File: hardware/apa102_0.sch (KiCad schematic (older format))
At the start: 77 parts

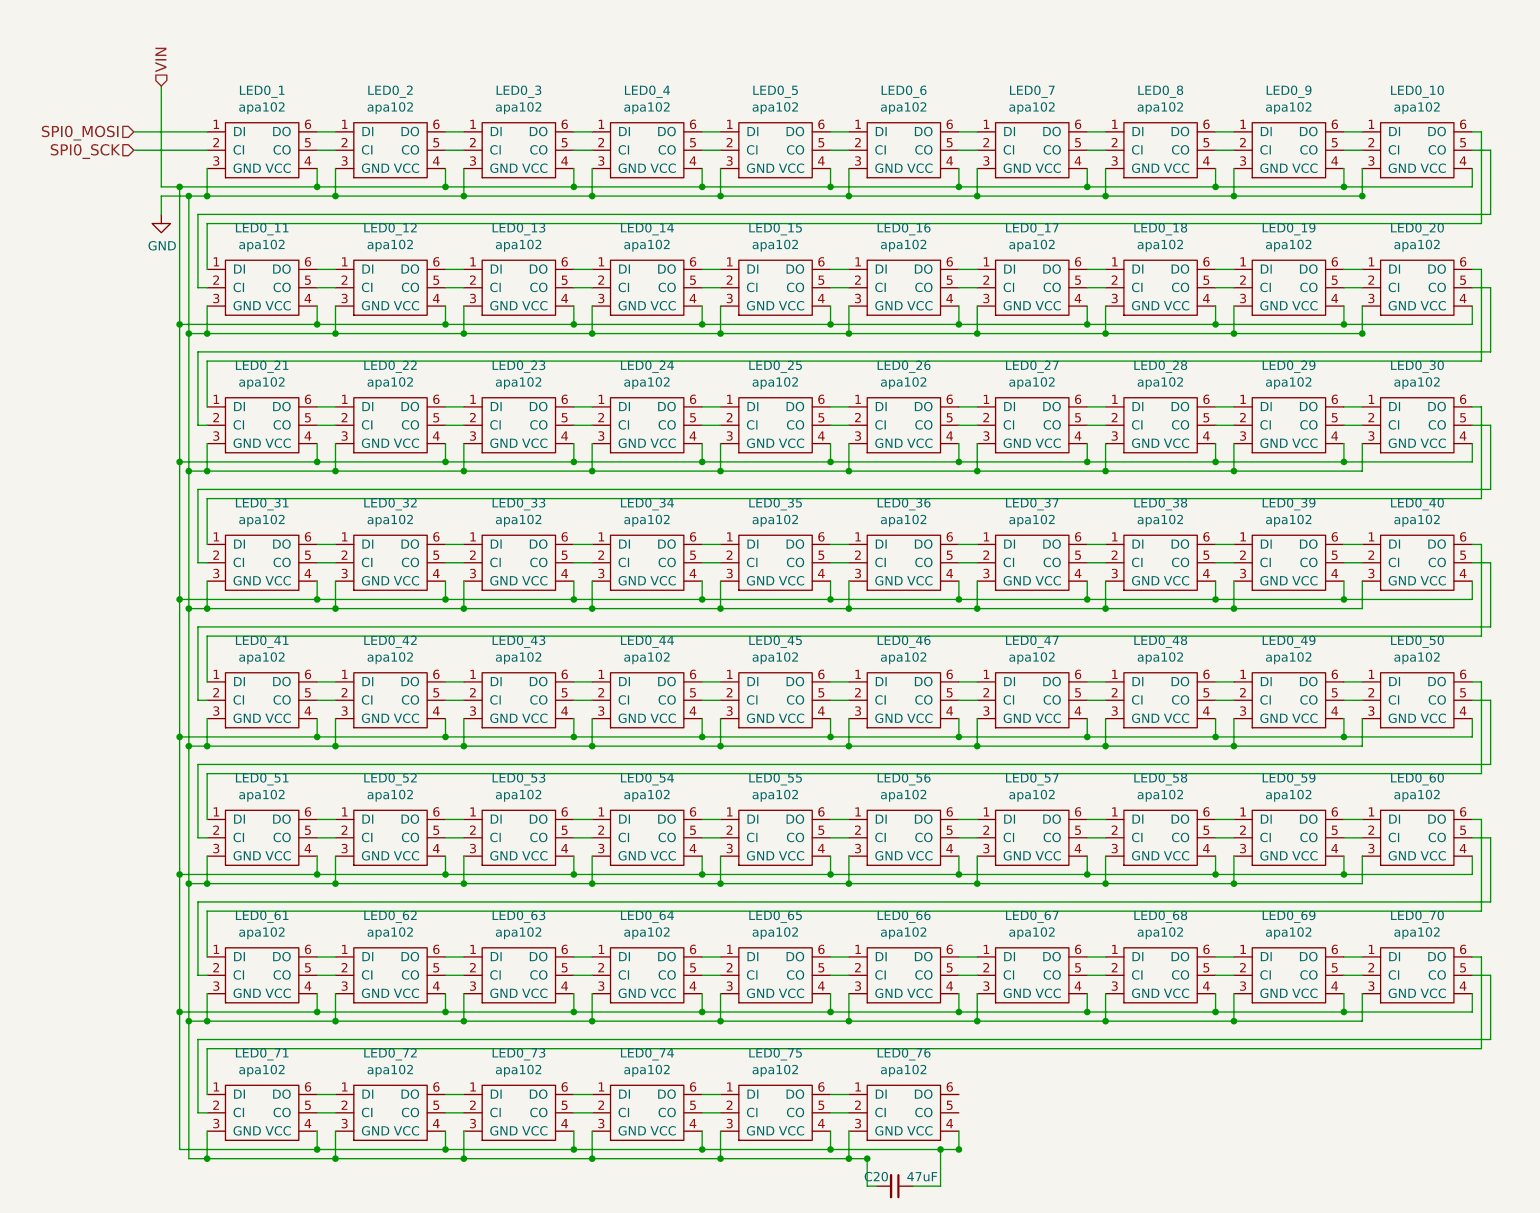
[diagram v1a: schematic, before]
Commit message: Removed 72 LEDs
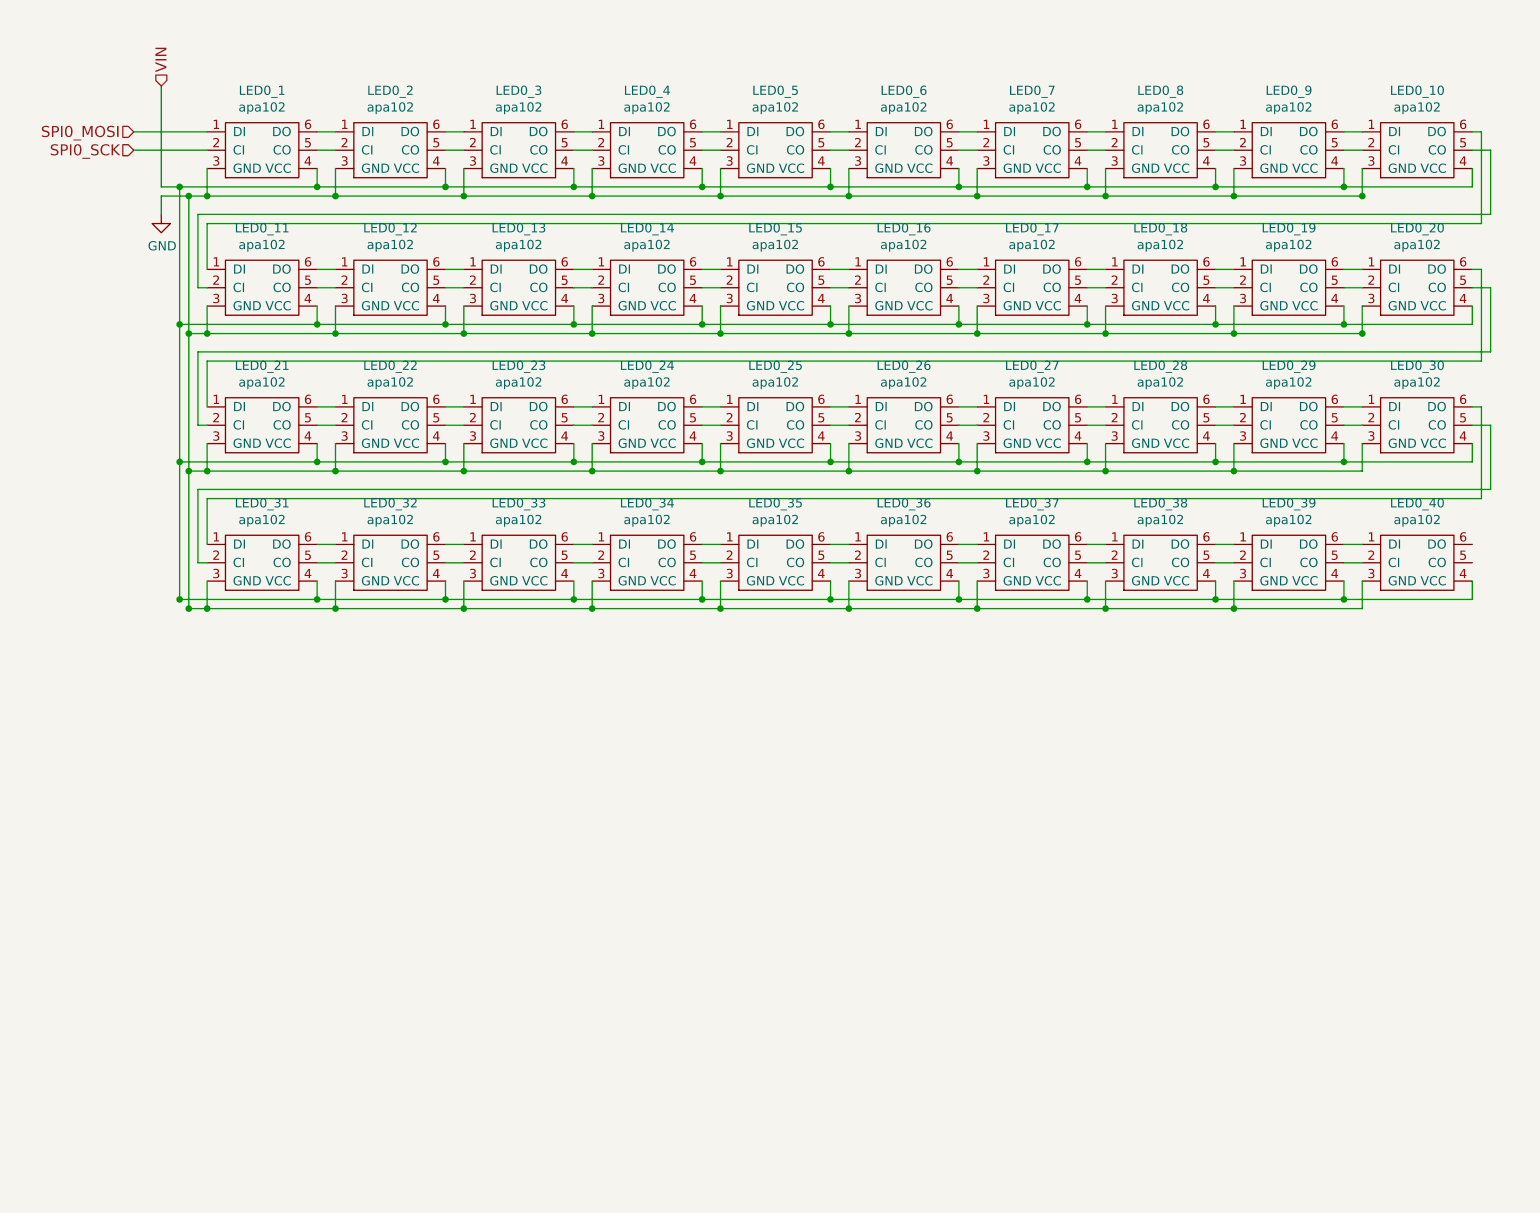
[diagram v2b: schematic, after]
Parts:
- removed C20: 47uF, Capacitors_SMD:C_0805, symbol C_Small
- removed LED0_41, LED0_42, LED0_43, LED0_44, LED0_45, LED0_46, LED0_47, LED0_48, LED0_49, LED0_50, LED0_51, LED0_52, LED0_53, LED0_54, LED0_55, LED0_56, LED0_57, LED0_58, LED0_59, LED0_60, LED0_61, LED0_62, LED0_63, LED0_64, LED0_65, LED0_66, LED0_67, LED0_68, LED0_69, LED0_70, LED0_71, LED0_72, LED0_73, LED0_74, LED0_75, LED0_76: apa102, apa102:apa102, symbol apa102

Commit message: Switched to fat small design
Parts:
- LED0_1, LED0_10, LED0_11, LED0_12, LED0_13, LED0_14, LED0_15, LED0_16, LED0_17, LED0_18, LED0_19, LED0_2, LED0_20, LED0_21, LED0_22, LED0_23, LED0_24, LED0_25, LED0_26, LED0_27, LED0_28, LED0_29, LED0_3, LED0_30, LED0_31, LED0_32, LED0_33, LED0_34, LED0_35, LED0_36, LED0_37, LED0_38, LED0_39, LED0_4, LED0_40, LED0_5, LED0_6, LED0_7, LED0_8, LED0_9: symbol apa102 -> APA102
